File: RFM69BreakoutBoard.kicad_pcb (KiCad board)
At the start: 2 copper layers, 26.2 x 25.8 mm, 21 parts, among them P1 BB Holes, P10 TST, P11 TST, P12 TST, P2 TST, P3 TST, P4 TST, P5 TST, P6 TST, P7 TST, P8 TST, P9 TST, U1 MCP1703, U2 74HCT123, U3 RFM69HW

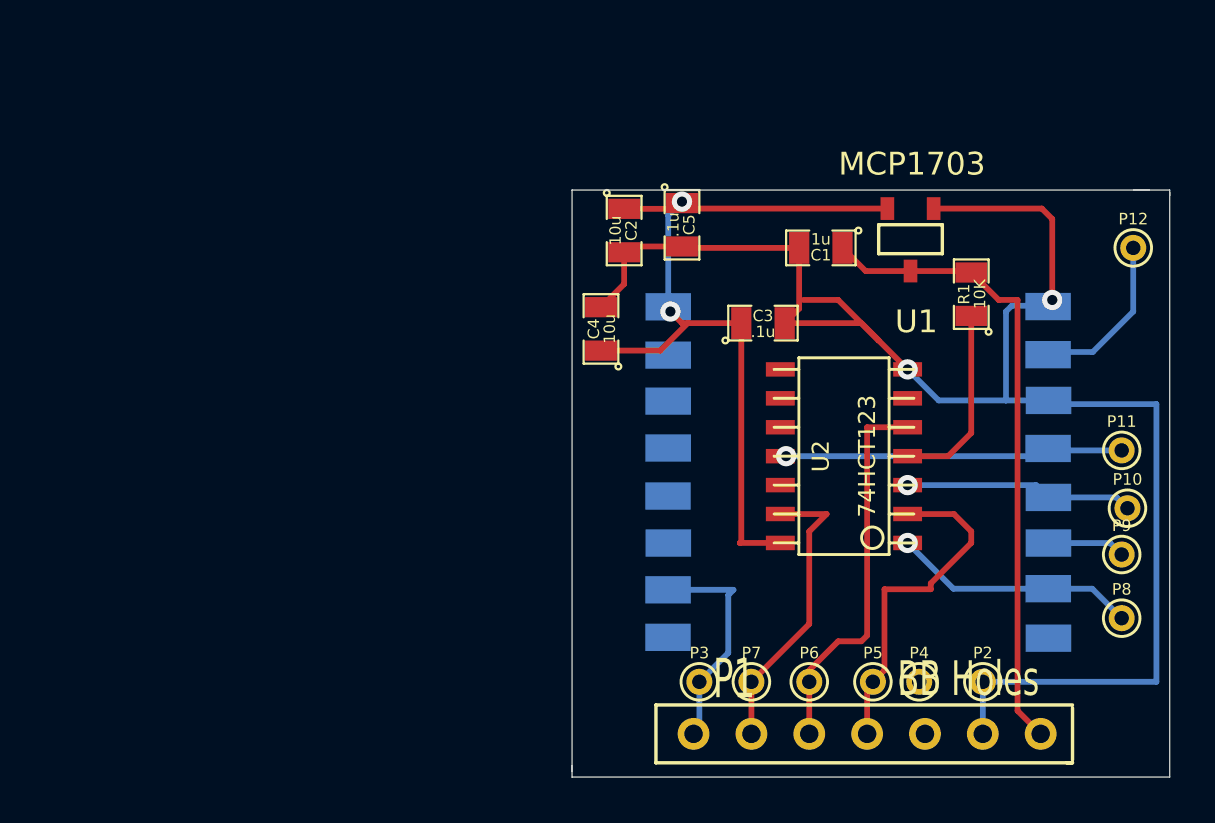
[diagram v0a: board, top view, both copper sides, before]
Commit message: notice errors in schematic - updated schematic to fix
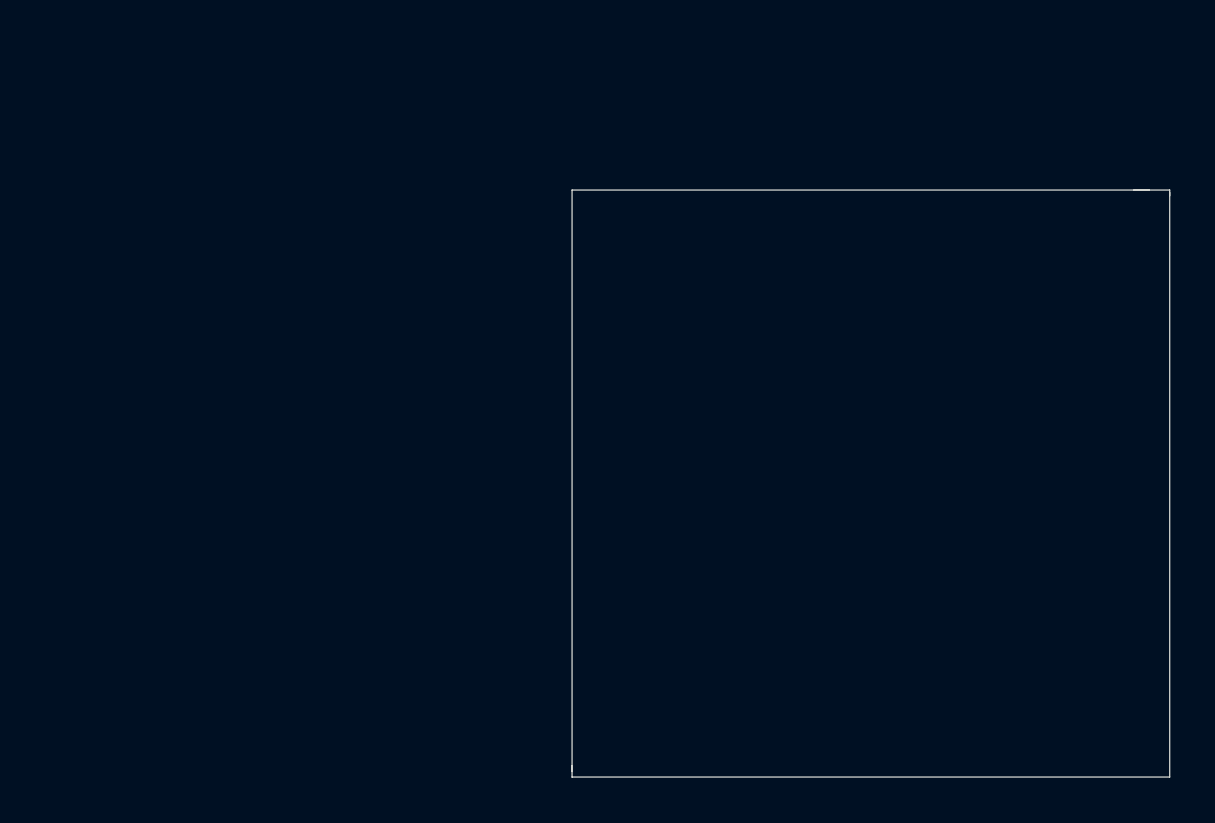
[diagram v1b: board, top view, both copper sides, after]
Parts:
- removed C1: 1u, SM0805
- removed C2, C4: 10u, SM0805
- removed C3, C5: .1u, SM0805
- removed P1: BB Holes, 7_PINS
- removed P10, P11, P12, P2, P3, P4, P5, P6, P7, P8, P9: TST, PINTST
- removed R1: 10K, SM0805
- removed U1: MCP1703, SOT-23A
- removed U2: 74HCT123, so-14
- removed U3: RFM69HW, RFM69HW
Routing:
- net GND: track 73.3 -> 0.00 mm, vias 2 -> 0
- net +3.3V: track 36.0 -> 0.00 mm, vias 2 -> 0
- net +5V: track 28.6 -> 0.00 mm
- net /CS_5V: track 21.4 -> 0.00 mm
- net /MOSI_5V: track 16.9 -> 0.00 mm
- net /CLK_3V3: track 15.2 -> 0.00 mm, vias 1 -> 0
- net /MISO: track 15.1 -> 0.00 mm
- net /CS_3V3: track 10.8 -> 0.00 mm, vias 1 -> 0
- net /MISO_3V3: track 10.1 -> 0.00 mm, vias 1 -> 0
- net /INT: track 9.92 -> 0.00 mm
- net /ANA: track 7.32 -> 0.00 mm
- net /MOSI_3V3: track 3.42 -> 0.00 mm

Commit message: first pass of trace
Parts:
- added C1: 1u, SM0805, B.Cu at (80.5, 153.4)
- added C2: 10u, SM0805, B.Cu at (80.5, 147.3)
- added C3: .1u, SM0805, B.Cu at (80.5, 151.4)
- added C4: 10u, SM0805, B.Cu at (80.5, 145.3)
- added C5: .1u, SM0805, B.Cu at (80.5, 143.3)
- added P1: BB Holes, 7_PINS, F.Cu at (67.3, 157.1)
- added P10: TST, PINTST, F.Cu at (80.8, 139.4)
- added P11: TST, PINTST, F.Cu at (80.8, 141.5)
- added P12: TST, PINTST, F.Cu at (80.5, 149.4)
- added P2: TST, PINTST, F.Cu at (73.7, 154.4)
- added P3: TST, PINTST, F.Cu at (61.0, 154.4)
- added P4: TST, PINTST, F.Cu at (71.1, 154.4)
- added P5: TST, PINTST, F.Cu at (68.6, 154.4)
- added P6: TST, PINTST, F.Cu at (66.0, 154.4)
- added P7: TST, PINTST, F.Cu at (63.5, 154.4)
- added P8: TST, PINTST, F.Cu at (80.8, 135.4)
- added P9: TST, PINTST, F.Cu at (80.8, 137.4)
- added R1: 10K, SM0805, F.Cu at (68.5, 142.7)
- added U1: MCP1703, SOT-23A, B.Cu at (79.2, 156.0)
- added U2: 74HCT123, so-14, B.Cu at (67.8, 143.0)
- added U3: RFM69HW, RFM69HW, F.Cu at (68.9, 144.4)
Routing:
- net +3.3V: track 0.00 -> 58.1 mm, vias 0 -> 1
- net GND: track 0.00 -> 37.5 mm, vias 0 -> 2
- net /CS_5V: track 0.00 -> 32.0 mm, vias 0 -> 1
- net +5V: track 0.00 -> 31.3 mm
- net /CLK_5V: track 0.00 -> 22.3 mm, vias 0 -> 1
- net /INT: track 0.00 -> 22.0 mm
- net /CS_3V3: track 0.00 -> 21.7 mm, vias 0 -> 1
- net /MOSI_3V3: track 0.00 -> 20.1 mm, vias 0 -> 1
- net /MOSI_5V: track 0.00 -> 14.2 mm
- net /MISO: track 0.00 -> 14.0 mm
- net /MISO_3V3: track 0.00 -> 13.7 mm, vias 0 -> 1
- net /CLK_3V3: track 0.00 -> 13.3 mm, vias 0 -> 1
- net /ANA: track 0.00 -> 3.23 mm
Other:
- board size 26.2 x 25.8 mm -> 25.4 x 25.4 mm
- net class Default: clearance 0.254 -> 0.1524; trace_width 0.254 -> 0.1524; via_dia 0.889 -> 0.508; via_drill 0.635 -> 0.3302
- rule trace_clearance: 0.254 -> 0.1524
- rule trace_min: 0.254 -> 0.1524
- rule via_min_drill: 0.508 -> 0.3302
- rule via_min_size: 0.889 -> 0.508
